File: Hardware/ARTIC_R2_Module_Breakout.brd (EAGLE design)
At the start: 27.9 x 50.8 mm, 36 parts, among them U1 2Mbit SPI Flash

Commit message: Final tweaks
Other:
- board text added: "2-Layer Board 1.6mm Thickness 1oz Copper (Outer layers) HASL Finish Pins are: 2 x PRT11541 2 x PRT11540"
- board text removed: "2-Layer Board 1.6mm Thickness 1oz Copper (Outer layers) HASL Finish"
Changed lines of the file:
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@@
 1oz Copper (Outer layers)
 HASL Finish
+Pins are:
+2 x PRT11541
+2 x PRT11540
 </text>
 <dimension x1="-2.54" y1="2.54" x2="25.4" y2="2.54" x3="11.43" y3="-7.62" textsize="1.778" textratio="15" layer="47" unit="inch"/>
@@
 <via x="17.78" y="34.29" extent="1-16" drill="0.299975"/>
 <via x="17.78" y="36.83" extent="1-16" drill="0.299975"/>
+<via x="-0.635" y="10.16" extent="1-16" drill="0.299975"/>
+<via x="-0.889" y="7.493" extent="1-16" drill="0.299975"/>
+<via x="16.764" y="1.016" extent="1-16" drill="0.299975"/>
+<via x="5.08" y="30.48" extent="1-16" drill="0.299975"/>
+<via x="8.89" y="30.48" extent="1-16" drill="0.299975"/>
+<via x="8.89" y="19.05" extent="1-16" drill="0.299975"/>
+<via x="13.97" y="24.13" extent="1-16" drill="0.299975"/>
+<via x="11.43" y="21.59" extent="1-16" drill="0.299975"/>
+<via x="5.08" y="15.24" extent="1-16" drill="0.299975"/>
 </signal>
 <signal name="EDAP">

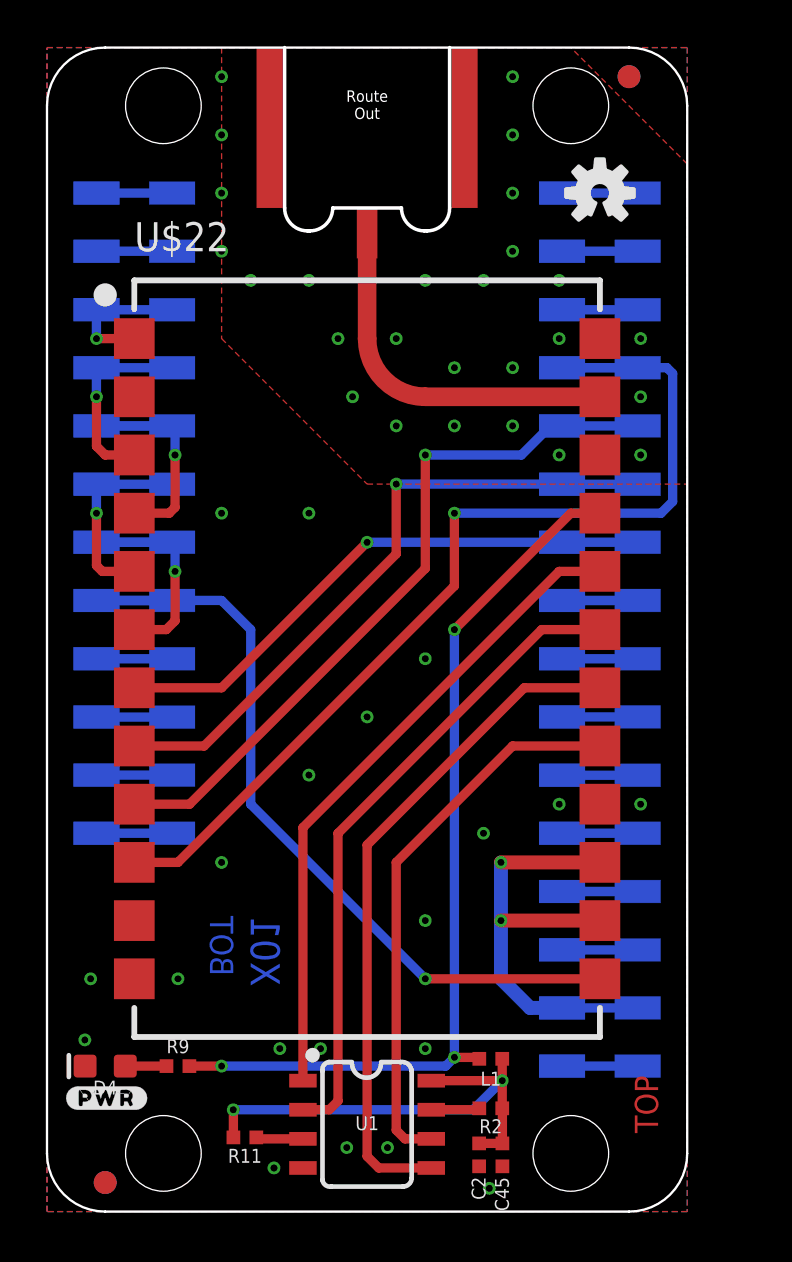
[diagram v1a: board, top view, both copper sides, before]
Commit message: Updates to match the revised module design
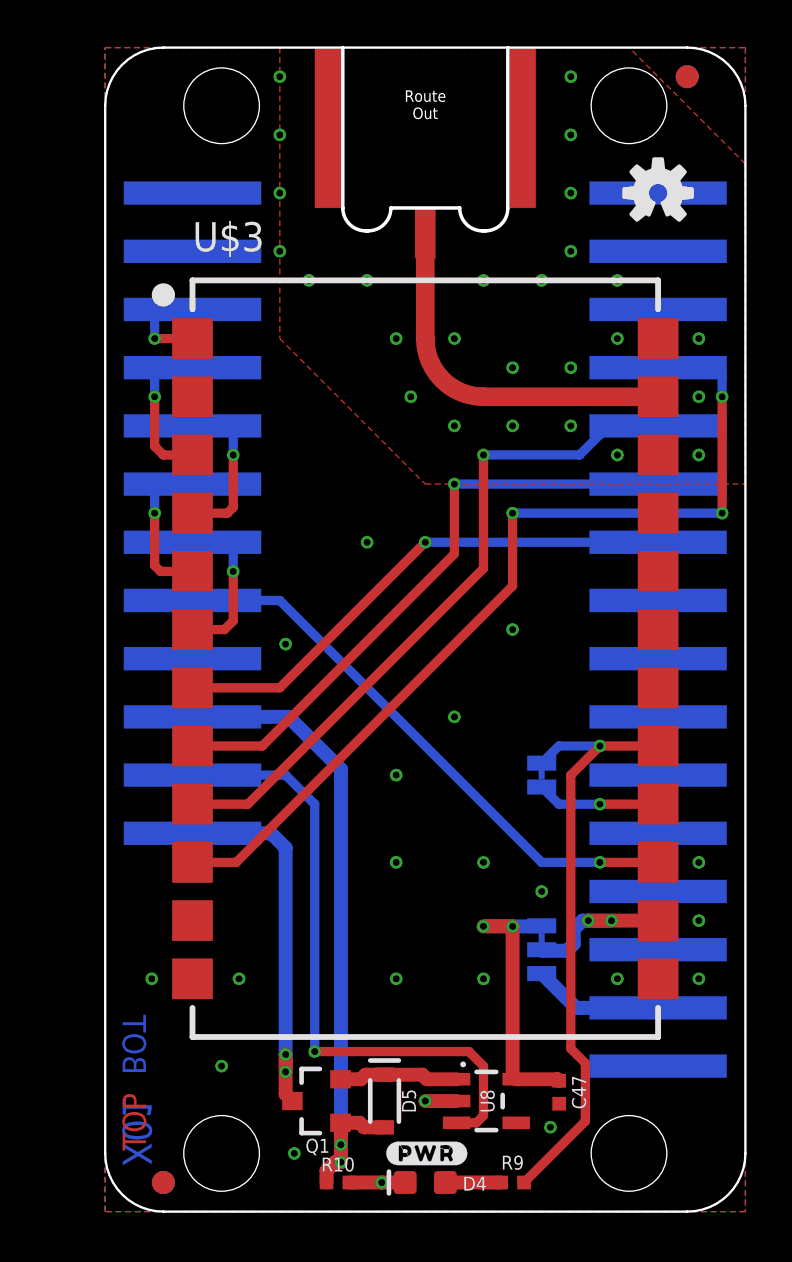
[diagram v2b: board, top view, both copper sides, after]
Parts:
- removed C2: 22pF, SparkFun-Capacitors:0402-TIGHT
- removed C45: 0.1uF, SparkFun-Capacitors:0402-TIGHT
- removed L1: 30Ω, SparkFun-Coils:0402-TIGHT
- removed R11, R2: 0, SparkFun-Resistors:0402-TIGHT
- removed U$22: ARTIC_R2_MODULE, ARTIC_R2_Module:ARTIC_R2_MODULE
- removed U1: 2Mbit SPI Flash, New_Parts_IC-Memory:SO08
- added C47: 2.2uF, SparkFun-Capacitors:0402-TIGHT
- added D5: 1A/23V/620mV, SparkFun-DiscreteSemi:SOD-323
- added J2: (no value), Connectors:1X06_SMD_MALE
- added JP1: JUMPER-SMT_2_NC_TRACE_SILK, SparkFun-Jumpers:SMT-JUMPER_2_NC_TRACE_SILK
- added JP2: JUMPER-SMT_3_1-NC_TRACE_SILK, SparkFun-Jumpers:SMT-JUMPER_3_1-NC_TRACE_SILK
- added Q1: 3.1A/30V/105mΩ, SparkFun-DiscreteSemi:SOT23-3
- added R10: 100k, SparkFun-Resistors:0402-TIGHT
- added U$3: ARTIC_R2_MODULE, ARTIC_R2_Module:ARTIC_R2_MODULE
- added U$4: (no value), output:#FLASH_PWR#0
- added U$5: (no value), output:#VBAT#0
- added U$7: (no value), output:#EN#0
- added U$8: (no value), output:#VUSB#0
- added U8: 3.3V, SparkFun-IC-Power:SOT23-5
- J1: device SparkFun-Connectors:1X12_SMD_COMBINED -> Connectors:1X06_SMD_MALE
- J3, J4: device SparkFun-Connectors:1X08_SMD_COMBINED -> Connectors:1X08_SMD_MALE
- moved SPARKX2 19.8 mm to (14.0, 2.54), turned to 0 degrees
- moved LOGO3 17.3 mm to (14.0, 5.46), turned to 0 degrees
- moved R9 15.5 mm to (17.8, 1.27)
- moved D4 14.9 mm to (14.0, 1.27)
- moved U$28 14.2 mm to (14.0, 2.54)
- moved U$29 2.84 mm to (15.2, 23.5)
- moved U$24 2.79 mm to (9.14, 36.8)
- moved U$26 2.79 mm to (8.70, 31.8)
- moved U$6 2.79 mm to (8.26, 39.4)
- moved U$18 2.79 mm to (9.84, 29.2)
- moved U$19 2.79 mm to (9.78, 26.7)
- moved U$25 2.79 mm to (8.57, 34.3)
- moved E1 2.54 mm to (14.0, 50.8)
- moved FD3 2.54 mm to (2.54, 1.27)
- moved FD4 2.54 mm to (2.54, 1.27)
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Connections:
- removed net FLSH_CEN: U$22.20, U1.1
- removed net FLSH_SCLK: U$22.17, U1.6
- removed net FLSH_SI: U$22.18, U1.5
- removed net FLSH_SO: U$22.19, U1.2
- removed net FLSH_VCC: C2.1, C45.1, L1.1, R11.2, R2.2, U1.8
- removed net N$1: E1.SIG, U$22.23
- removed net N$2: R2.1, U1.7
- removed net N$3: R11.1, U1.3
- removed net VDD: L1.2, R9.2, U$22.21
- new net 3.3V_OUT: JP1.1, R9.2, U$3.17
- new net ANTENNA: E1.SIG, U$3.23
- new net EN: J2.5, U8.3
- new net FLASH_PWR: JP1.2, U$3.16
- new net VCC_1: C47.1, JP2.3, U8.5
- new net VCC_2: J4.7, JP2.1
- new net VIN: D5.C, Q1.2, U8.1
- new net V_BATT: J2.6, Q1.3
- new net V_USB: D5.A, J2.4, Q1.1, R10.2
- net 3.3V: now also JP2.2, U$3.14; no longer J4.7, U$22.14, U$22.15
- net BOOT: now also U$3.3; no longer U$22.3
- net CIPO: now also U$3.10; no longer U$22.10
- net COPI: now also U$3.9; no longer U$22.9
- net CS: now also U$3.7; no longer U$22.7
- net G8: now also U$3.1; no longer U$22.1
- net GND: now also C47.2, R10.1, U$3.12, U$3.13, U$3.22, U$3.24, U8.2; no longer C2.2, C45.2, U$22.12, U$22.16, U$22.22, U$22.24, U1.4
- net INT1: now also U$3.4; no longer U$22.4
- net INT2: now also U$3.5; no longer U$22.5
- net PWR_EN: now also J2.2, U$3.15; no longer J1.8, U$22.13
- net RESETB: now also J2.1, U$3.6; no longer J1.7, U$22.6
- net SCLK: now also U$3.8; no longer U$22.8
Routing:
- net VDD: track 40.0 -> 0.00 mm, vias 3 -> 0
- net FLSH_SI: track 29.6 -> 0.00 mm
- net V_USB: track 0.00 -> 29.6 mm, vias 0 -> 2
- net FLSH_CEN: track 28.6 -> 0.00 mm
- net FLSH_SO: track 28.5 -> 0.00 mm
- net EN: track 0.00 -> 27.7 mm, vias 0 -> 1
- net 3.3V_OUT: track 0.00 -> 26.3 mm, vias 0 -> 1
- net FLSH_SCLK: track 24.4 -> 0.00 mm
- net FLSH_VCC: track 21.3 -> 0.00 mm, vias 2 -> 0
- net V_BATT: track 0.00 -> 16.3 mm, vias 0 -> 2
- net N$1: track 15.8 -> 0.00 mm
- net ANTENNA: track 0.00 -> 15.8 mm
- net VCC_1: track 0.00 -> 12.5 mm, vias 0 -> 2
- net 3.3V: track 16.9 -> 7.03 mm
- net PWR_EN: track 33.3 -> 25.1 mm
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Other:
- board text added: "2-Layer Board 1.6mm Thickness 1oz Copper (Outer layers) HASL Finish"
- board text removed: "2-Layer Board 1.6mm Thickness 1oz Copper (Outer layers) HASL Finish Pins are: 2 x PRT11541 2 x PRT11540"
